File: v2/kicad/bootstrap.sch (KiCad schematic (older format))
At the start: 3 parts, among them U5 74HC595, U6 74HC595

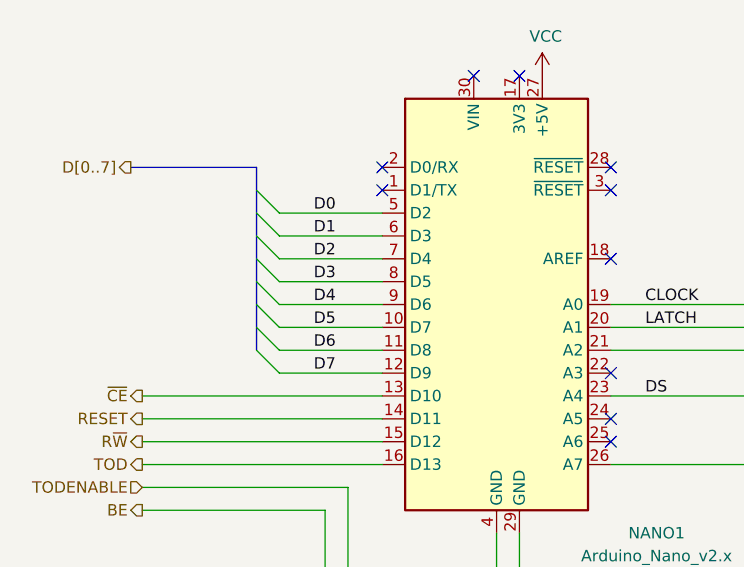
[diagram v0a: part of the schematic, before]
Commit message: Changing to Dual CIA
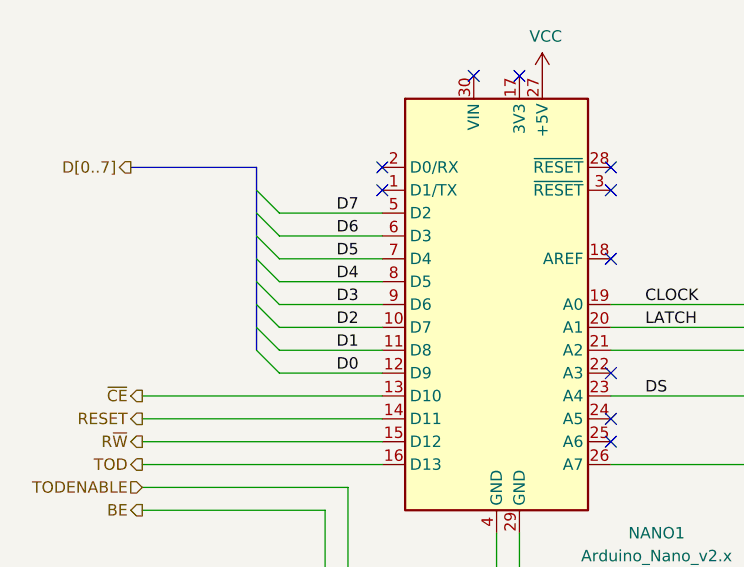
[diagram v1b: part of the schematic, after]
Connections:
- net D0: now also NANO1.12 (D9); no longer NANO1.5 (D2)
- net D1: now also NANO1.11 (D8); no longer NANO1.6 (D3)
- net D2: now also NANO1.10 (D7); no longer NANO1.7 (D4)
- net D3: now also NANO1.9 (D6); no longer NANO1.8 (D5)
- net D4: now also NANO1.8 (D5); no longer NANO1.9 (D6)
- net D5: now also NANO1.7 (D4); no longer NANO1.10 (D7)
- net D6: now also NANO1.6 (D3); no longer NANO1.11 (D8)
- net D7: now also NANO1.5 (D2); no longer NANO1.12 (D9)
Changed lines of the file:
@@
 Entry Wire Line
 	3500 3150 3400 3050
-Text Label 3650 3150 0    50   ~ 0
-D0
-Text Label 3650 3250 0    50   ~ 0
-D1
-Text Label 3650 3350 0    50   ~ 0
-D2
-Text Label 3650 3450 0    50   ~ 0
-D3
-Text Label 3650 3550 0    50   ~ 0
-D4
-Text Label 3650 3650 0    50   ~ 0
-D5
-Text Label 3650 3750 0    50   ~ 0
-D6
-Text Label 3650 3850 0    50   ~ 0
-D7
 Wire Bus Line
 	2850 2950 3400 2950
@@
 Wire Bus Line
 	8950 1750 8950 5200
+Text Label 3750 3150 0    50   ~ 0
+D7
+Text Label 3750 3250 0    50   ~ 0
+D6
+Text Label 3750 3350 0    50   ~ 0
+D5
+Text Label 3750 3450 0    50   ~ 0
+D4
+Text Label 3750 3550 0    50   ~ 0
+D3
+Text Label 3750 3650 0    50   ~ 0
+D2
+Text Label 3750 3750 0    50   ~ 0
+D1
+Text Label 3750 3850 0    50   ~ 0
+D0
 $EndSCHEMATC
